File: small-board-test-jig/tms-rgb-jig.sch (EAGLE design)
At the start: 15 parts, among them J10 R, J11 G, J12 B, J13 S_75, J14 GND, J15 S_TTL, J16 PIN1, J4 R-Y, J5 B-Y, J6 Y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

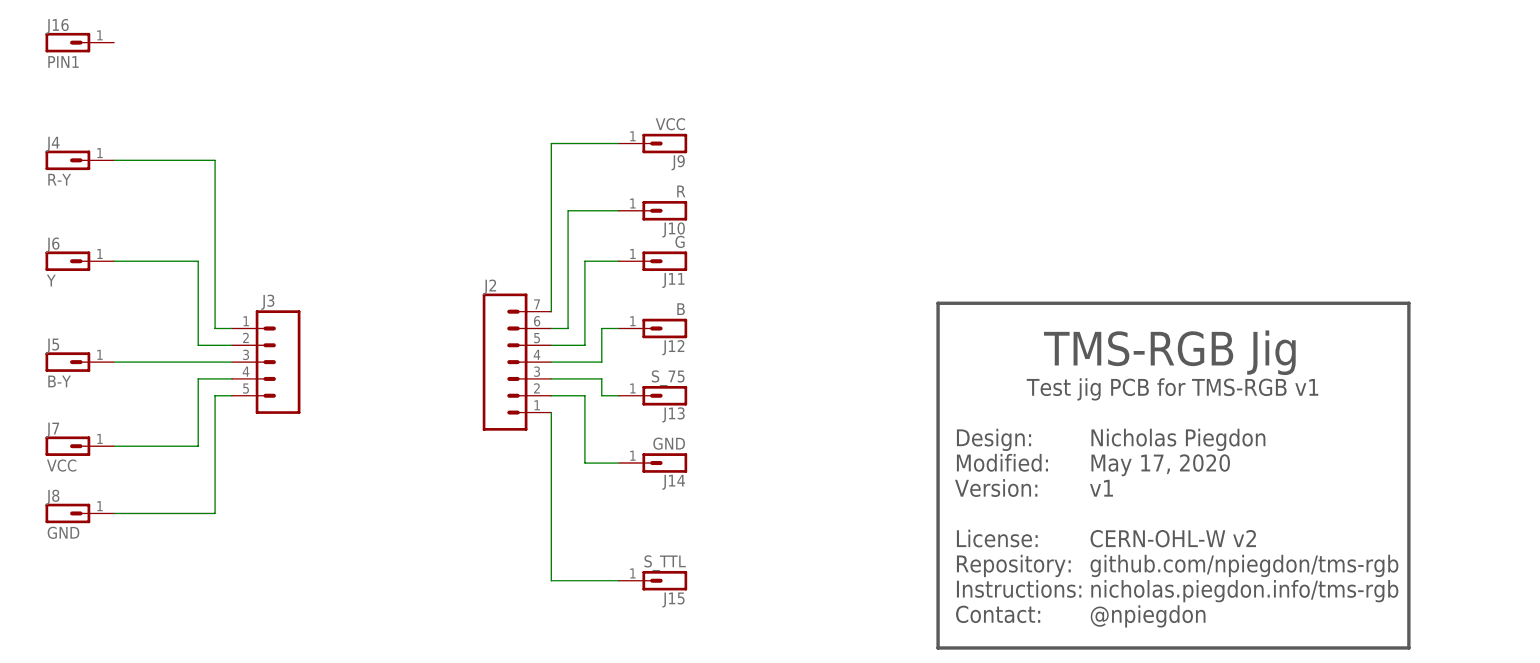
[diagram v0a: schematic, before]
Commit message: Update jig for v2
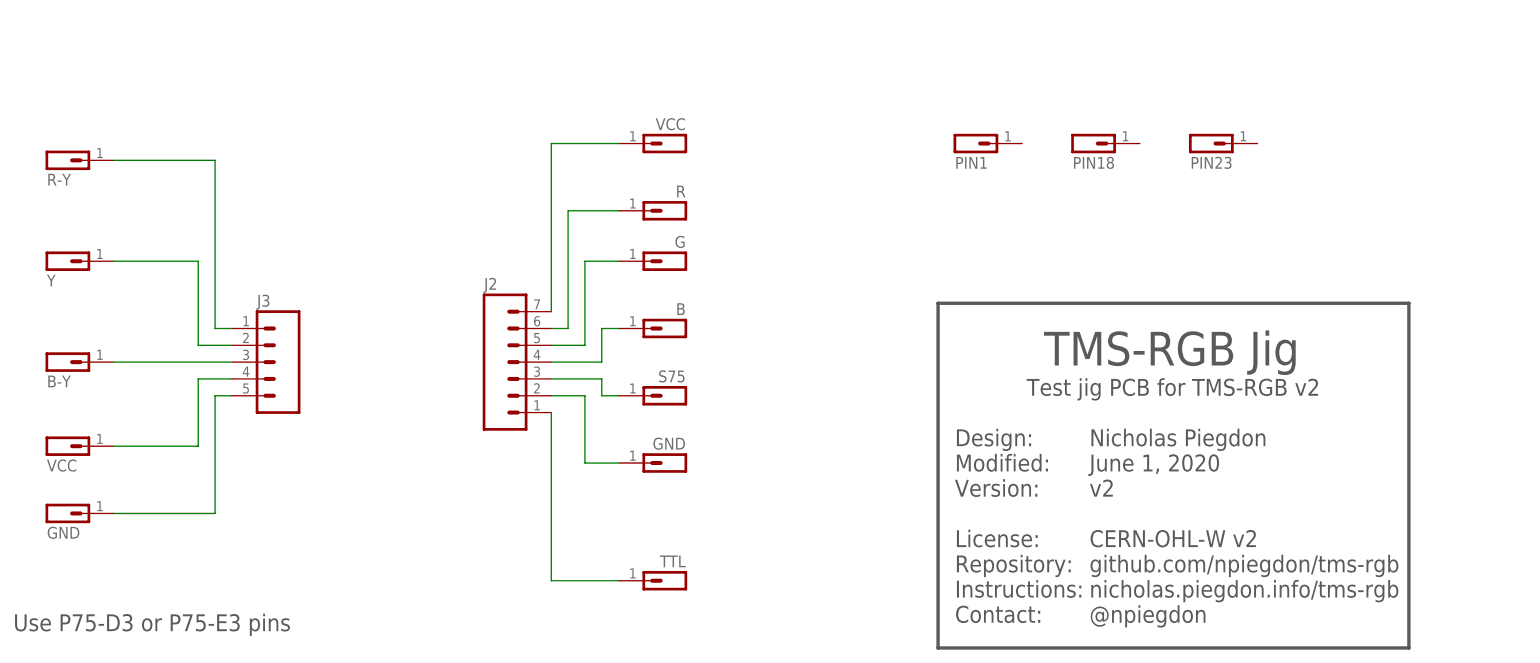
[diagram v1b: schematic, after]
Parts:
- added J17: PIN18, tms-rgb-jig:CONN_POGO
- added J18: PIN23, tms-rgb-jig:CONN_POGO
- J13: value S_75 -> S75
- J15: value S_TTL -> TTL
- J2: value (none) -> CONN_07
- J3: value (none) -> CONN_05
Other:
- note added: "Nicholas Piegdon June 1, 2020 v2 CERN-OHL-W v2 github.com/npiegdon/tms-rgb nicholas.piegdon.info/tms-rgb @npiegdon"
- note added: "Test jig PCB for TMS-RGB v2"
- note added: "Use P75-D3 or P75-E3 pins"
- note removed: "Nicholas Piegdon May 17, 2020 v1 CERN-OHL-W v2 github.com/npiegdon/tms-rgb nicholas.piegdon.info/tms-rgb @npiegdon"
- note removed: "Test jig PCB for TMS-RGB v1"
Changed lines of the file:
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@@
 <part name="J11" library="tms-rgb-jig" deviceset="CONN_POGO" device="" value="G"/>
 <part name="J12" library="tms-rgb-jig" deviceset="CONN_POGO" device="" value="B"/>
-<part name="J13" library="tms-rgb-jig" deviceset="CONN_POGO" device="" value="S_75"/>
+<part name="J13" library="tms-rgb-jig" deviceset="CONN_POGO" device="" value="S75"/>
 <part name="J14" library="tms-rgb-jig" deviceset="CONN_POGO" device="" value="GND"/>
-<part name="J15" library="tms-rgb-jig" deviceset="CONN_POGO" device="" value="S_TTL"/>
+<part name="J15" library="tms-rgb-jig" deviceset="CONN_POGO" device="" value="TTL"/>
 <part name="J16" library="tms-rgb-jig" deviceset="CONN_POGO" device="" value="PIN1"/>
+<part name="J17" library="tms-rgb-jig" deviceset="CONN_POGO" device="" value="PIN18"/>
+<part name="J18" library="tms-rgb-jig" deviceset="CONN_POGO" device="" value="PIN23"/>
 </parts>
 <sheets>
@@
 <plain>
 <text x="165.1" y="33.02" size="2.54" layer="97" align="top-left">Nicholas Piegdon
-May 17, 2020
-v1
+June 1, 2020
+v2
 CERN-OHL-W v2
 github.com/npiegdon/tms-rgb
@@
 <wire x1="213.36" y1="0" x2="213.36" y2="52.07" width="0.508" layer="97"/>
 <wire x1="213.36" y1="52.07" x2="142.24" y2="52.07" width="0.508" layer="97"/>
-<text x="177.8" y="38.1" size="2.54" layer="97" align="bottom-center">Test jig PCB for TMS-RGB v1</text>
+<text x="177.8" y="38.1" size="2.54" layer="97" align="bottom-center">Test jig PCB for TMS-RGB v2</text>
 <text x="177.546" y="42.672" size="5.08" layer="97" align="bottom-center">TMS-RGB Jig</text>
+<text x="2.54" y="2.54" size="2.54" layer="97">Use P75-D3 or P75-E3 pins</text>
 </plain>
 <instances>
 <instance part="J2" gate="G$1" x="78.74" y="40.64" smashed="yes">
-<attribute name="VALUE" x="73.66" y="30.734" size="1.778" layer="96" font="vector"/>
-<attribute name="NAME" x="73.66" y="53.848" size="1.778" layer="95" font="vector"/>
+<attribute name="NAME" x="73.66" y="54.102" size="1.778" layer="95" font="vector"/>
 </instance>
 <instance part="J3" gate="G$1" x="43.18" y="43.18" smashed="yes" rot="R180">
-<attribute name="VALUE" x="45.72" y="53.086" size="1.778" layer="96" font="vector" rot="R180"/>
-<attribute name="NAME" x="42.164" y="53.34" size="1.778" layer="95" font="vector" rot="R180"/>
+<attribute name="NAME" x="39.37" y="51.562" size="1.778" layer="95" font="vector"/>
 </instance>
 <instance part="J4" gate="G$1" x="7.62" y="76.2" smashed="yes">
 <attribute name="VALUE" x="7.62" y="69.85" size="1.778" layer="96" font="vector"/>
-<attribute name="NAME" x="7.62" y="75.438" size="1.778" layer="95" font="vector"/>
 </instance>
 <instance part="J5" gate="G$1" x="7.62" y="45.72" smashed="yes">
 <attribute name="VALUE" x="7.62" y="39.37" size="1.778" layer="96" font="vector"/>
-<attribute name="NAME" x="7.62" y="44.958" size="1.778" layer="95" font="vector"/>
 </instance>
 <instance part="J6" gate="G$1" x="7.62" y="60.96" smashed="yes">
 <attribute name="VALUE" x="7.62" y="54.61" size="1.778" layer="96" font="vector"/>
-<attribute name="NAME" x="7.62" y="60.198" size="1.778" layer="95" font="vector"/>
 </instance>
 <instance part="J7" gate="G$1" x="7.62" y="33.02" smashed="yes">
 <attribute name="VALUE" x="7.62" y="26.67" size="1.778" layer="96" font="vector"/>
-<attribute name="NAME" x="7.62" y="32.258" size="1.778" layer="95" font="vector"/>
 </instance>
 <instance part="J8" gate="G$1" x="7.62" y="22.86" smashed="yes">
 <attribute name="VALUE" x="7.62" y="16.51" size="1.778" layer="96" font="vector"/>
-<attribute name="NAME" x="7.62" y="22.098" size="1.778" layer="95" font="vector"/>
 </instance>
 <instance part="J9" gate="G$1" x="104.14" y="73.66" smashed="yes" rot="R180">
 <attribute name="VALUE" x="104.14" y="80.01" size="1.778" layer="96" font="vector" rot="R180"/>
-<attribute name="NAME" x="104.14" y="74.422" size="1.778" layer="95" font="vector" rot="R180"/>
 </instance>
 <instance part="J10" gate="G$1" x="104.14" y="63.5" smashed="yes" rot="R180">
 <attribute name="VALUE" x="104.14" y="69.85" size="1.778" layer="96" font="vector" rot="R180"/>
-<attribute name="NAME" x="104.14" y="64.262" size="1.778" layer="95" font="vector" rot="R180"/>
 </instance>
 <instance part="J11" gate="G$1" x="104.14" y="55.88" smashed="yes" rot="R180">
 <attribute name="VALUE" x="104.14" y="62.23" size="1.778" layer="96" font="vector" rot="R180"/>
-<attribute name="NAME" x="104.14" y="56.642" size="1.778" layer="95" font="vector" rot="R180"/>
 </instance>
 <instance part="J12" gate="G$1" x="104.14" y="45.72" smashed="yes" rot="R180">
 <attribute name="VALUE" x="104.14" y="52.07" size="1.778" layer="96" font="vector" rot="R180"/>
-<attribute name="NAME" x="104.14" y="46.482" size="1.778" layer="95" font="vector" rot="R180"/>
 </instance>
 <instance part="J13" gate="G$1" x="104.14" y="35.56" smashed="yes" rot="R180">
 <attribute name="VALUE" x="104.14" y="41.91" size="1.778" layer="96" font="vector" rot="R180"/>
-<attribute name="NAME" x="104.14" y="36.322" size="1.778" layer="95" font="vector" rot="R180"/>
 </instance>
 <instance part="J14" gate="G$1" x="104.14" y="25.4" smashed="yes" rot="R180">
 <attribute name="VALUE" x="104.14" y="31.75" size="1.778" layer="96" font="vector" rot="R180"/>
-<attribute name="NAME" x="104.14" y="26.162" size="1.778" layer="95" font="vector" rot="R180"/>
 </instance>
 <instance part="J15" gate="G$1" x="104.14" y="7.62" smashed="yes" rot="R180">
 <attribute name="VALUE" x="104.14" y="13.97" size="1.778" layer="96" font="vector" rot="R180"/>
-<attribute name="NAME" x="104.14" y="8.382" size="1.778" layer="95" font="vector" rot="R180"/>
-</instance>
-<instance part="J16" gate="G$1" x="7.62" y="93.98" smashed="yes">
-<attribute name="VALUE" x="7.62" y="87.63" size="1.778" layer="96" font="vector"/>
-<attribute name="NAME" x="7.62" y="93.218" size="1.778" layer="95" font="vector"/>
+</instance>
+<instance part="J16" gate="G$1" x="144.78" y="78.74" smashed="yes">
+<attribute name="VALUE" x="144.78" y="72.39" size="1.778" layer="96" font="vector"/>
+</instance>
+<instance part="J17" gate="G$1" x="162.56" y="78.74" smashed="yes">
+<attribute name="VALUE" x="162.56" y="72.39" size="1.778" layer="96" font="vector"/>
+</instance>
+<instance part="J18" gate="G$1" x="180.34" y="78.74" smashed="yes">
+<attribute name="VALUE" x="180.34" y="72.39" size="1.778" layer="96" font="vector"/>
 </instance>
 </instances>
@@
 </sheet>
 </sheets>
+<errors>
+</errors>
 </schematic>
 </drawing>
